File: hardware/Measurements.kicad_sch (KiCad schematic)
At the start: 13 parts, among them IC1 MCP1501-10E_SN, IC3 REF193GSZ-REEL, IC7 MCP3562T-E_NC

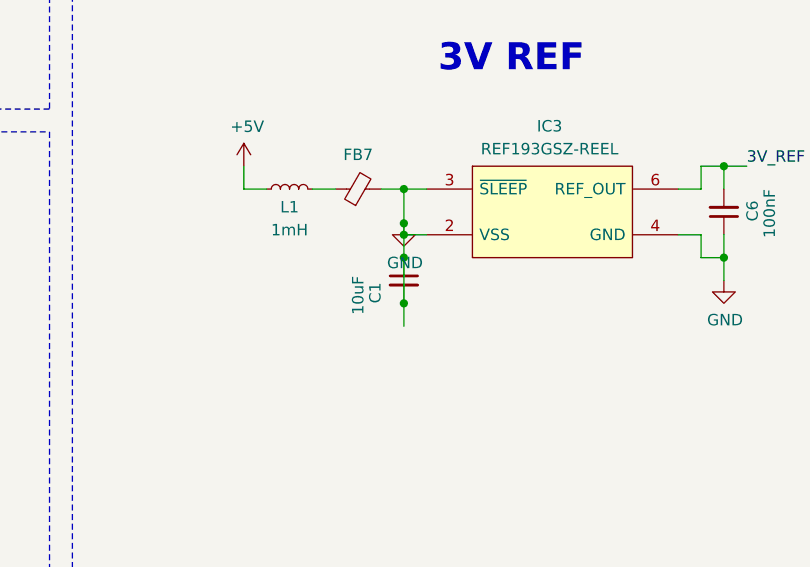
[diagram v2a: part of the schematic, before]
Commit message: relay new driving logic, some ltc communication changes
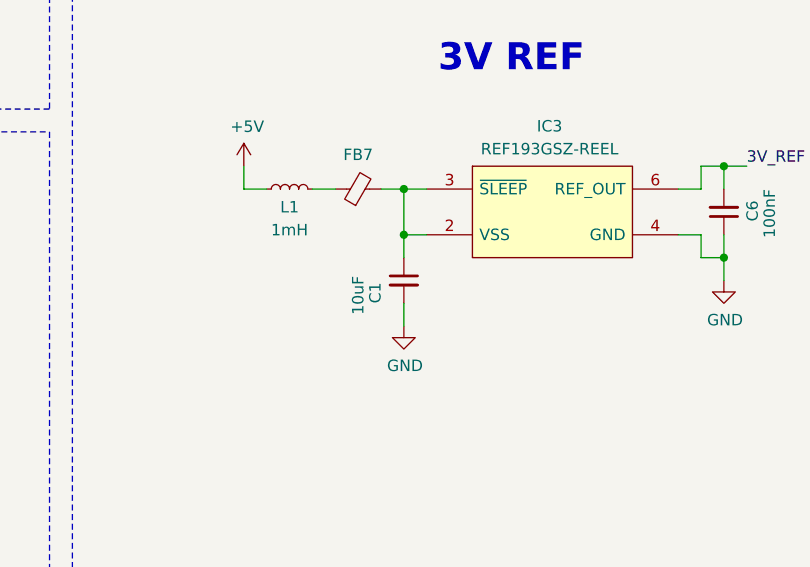
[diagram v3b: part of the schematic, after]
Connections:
- net GND: no longer C1.1, FB7.2, IC3.2 (VSS), IC3.3 (~{SLEEP})
- new net: C1.1, FB7.2, IC3.2 (VSS), IC3.3 (~{SLEEP})
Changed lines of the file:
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@@
-	)
-	(junction
-		(at 213.36 124.46)
-		(diameter 0)
-		(color 0 0 0 0)
-	)
-	(junction
-		(at 213.36 128.27)
-		(diameter 0)
-		(color 0 0 0 0)
 	)
 	(junction
@@
 	)
 	(junction
-		(at 213.36 133.35)
-		(diameter 0)
-		(color 0 0 0 0)
-	)
-	(junction
 		(at 213.36 125.73)
 		(diameter 0)
@@
 	(wire
 		(pts
-			(xy 213.36 133.35) (xy 213.36 128.27)
-		)
-		(stroke
-			(width 0)
-			(type default)
-		)
-	)
-	(wire
-		(pts
 			(xy 246.38 118.11) (xy 248.92 118.11)
 		)
@@
 	(wire
 		(pts
-			(xy 213.36 125.73) (xy 213.36 124.46)
+			(xy 213.36 120.65) (xy 213.36 125.73)
 		)
 		(stroke
@@
 		(pts
 			(xy 76.2 176.53) (xy 78.74 176.53)
-		)
-		(stroke
-			(width 0)
-			(type default)
-		)
-	)
-	(wire
-		(pts
-			(xy 213.36 124.46) (xy 213.36 120.65)
 		)
 		(stroke
@@
 	(symbol
 		(lib_id "power:GND")
-		(at 213.36 124.46 0)
+		(at 213.36 135.89 0)
 		(unit 1)
 		(exclude_from_sim no)
@@
 		(dnp no)
 		(property "Reference" "#PWR023"
-			(at 213.36 130.81 0)
+			(at 213.36 142.24 0)
 			(effects
 				(font
@@
 		)
 		(property "Value" "GND"
-			(at 213.487 128.8542 0)
+			(at 213.487 140.2842 0)
 			(effects
 				(font
@@
 		)
 		(property "Footprint" ""
-			(at 213.36 124.46 0)
+			(at 213.36 135.89 0)
 			(effects
 				(font
@@
 		)
 		(property "Datasheet" ""
-			(at 213.36 124.46 0)
+			(at 213.36 135.89 0)
 			(effects
 				(font
@@
 		)
 		(property "Description" ""
-			(at 213.36 124.46 0)
-			(effects
-				(font
+			(at 213.36 135.89 0)
+			(effects
+				(font

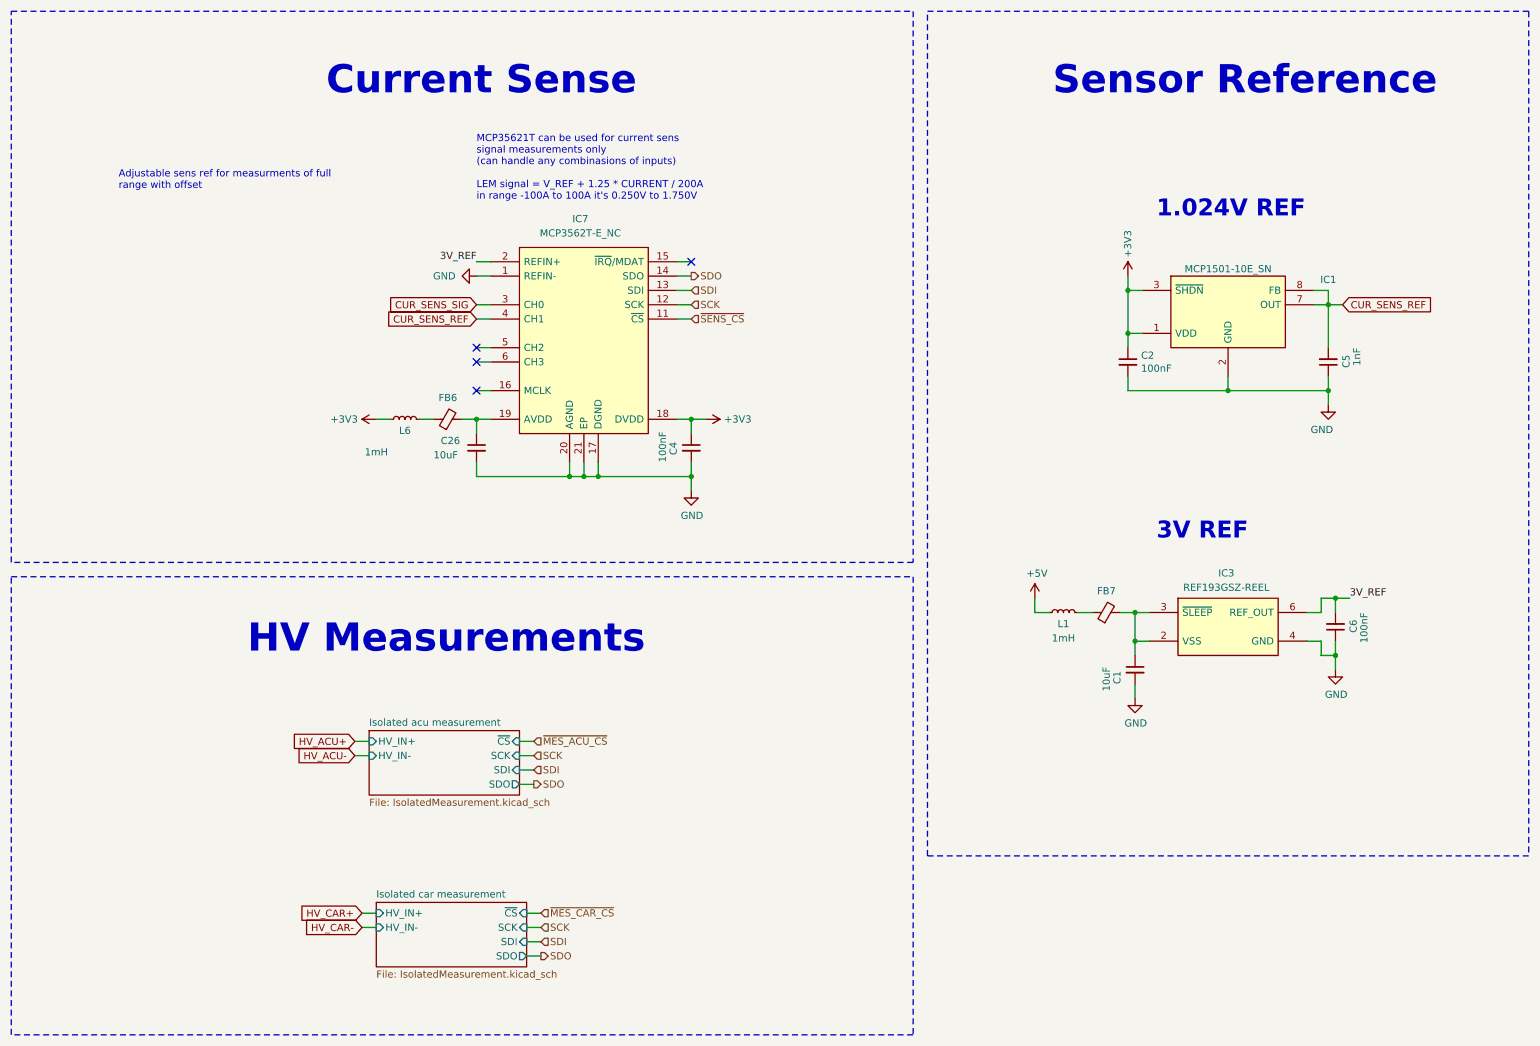
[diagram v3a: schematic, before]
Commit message: relay new driving logic, some ltc communication changes
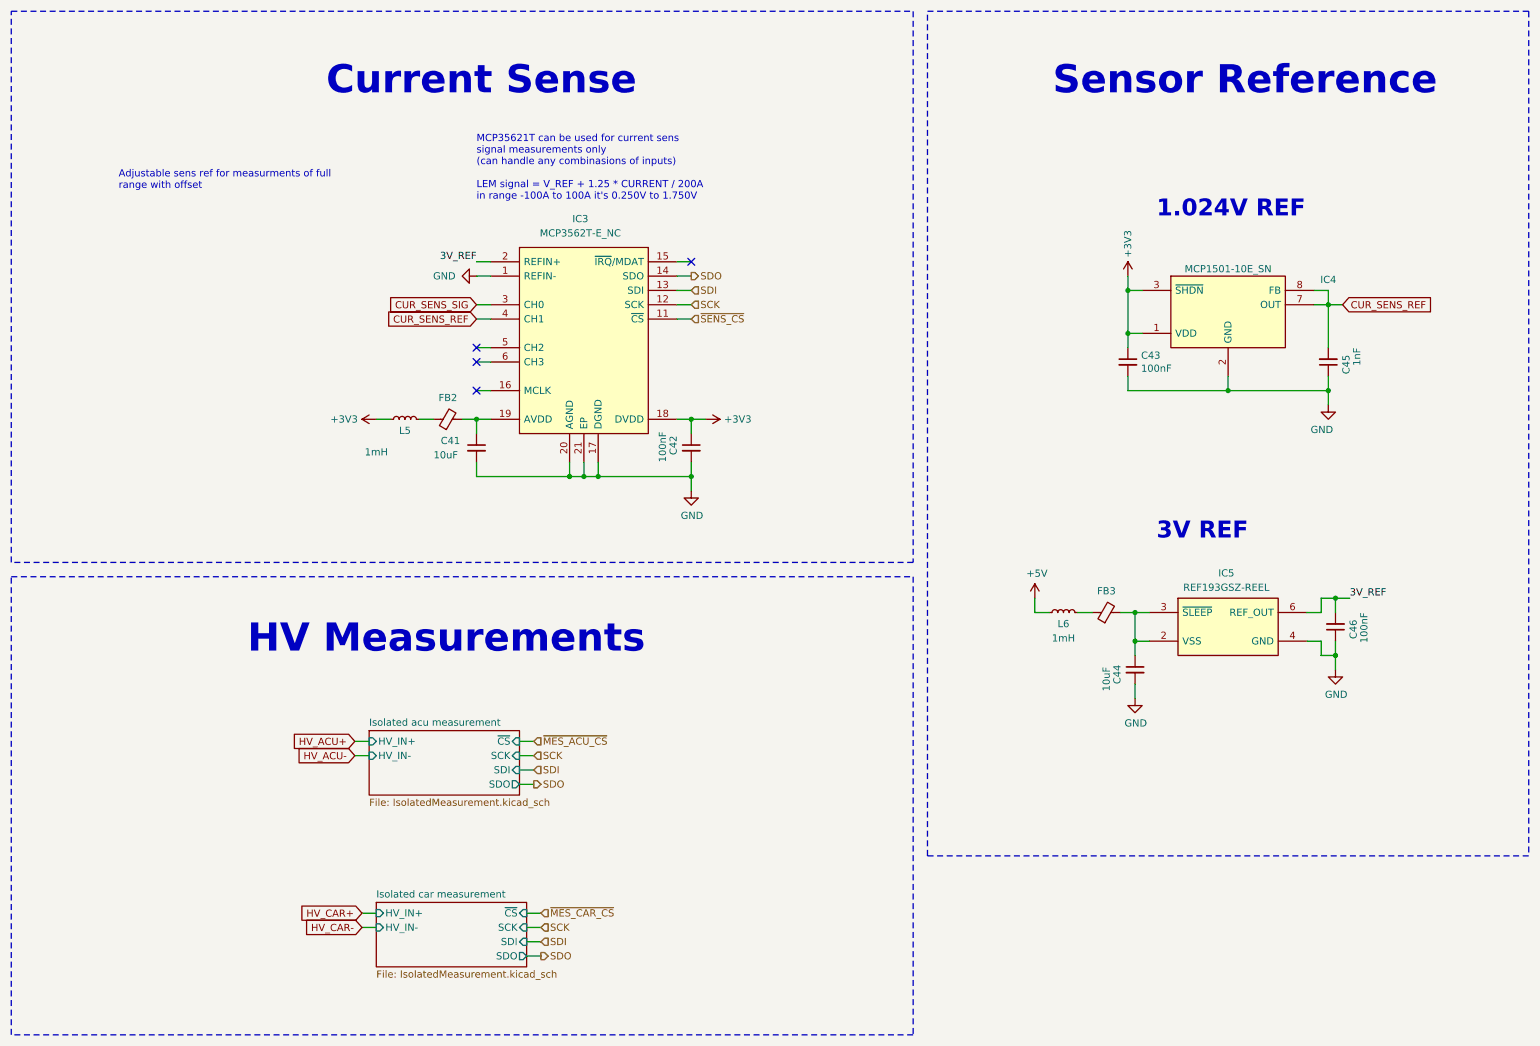
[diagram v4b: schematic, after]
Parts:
- renumbered C26 to C41, C4 to C42, C2 to C43, C1 to C44, C5 to C45, C6 to C46, FB6 to FB2, FB7 to FB3, IC7 to IC3, IC1 to IC4, IC3 to IC5, L6 to L5, L1 to L6
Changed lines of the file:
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@@
 		(on_board yes)
 		(dnp no)
-		(property "Reference" "C1"
+		(property "Reference" "C44"
 			(at 210.185 133.35 90)
 			(effects
@@
 			(project "PUTM_EV_BMS_HV_Master_2021"
 				(path "/b456cffc-d9d7-4c91-91f2-36ec9a65dd1b/e61cc821-5479-4c04-b5ab-4a32f17b4f03"
-					(reference "C1")
+					(reference "C44")
 					(unit 1)
 				)
@@
 		(on_board yes)
 		(dnp no)
-		(property "Reference" "IC1"
+		(property "Reference" "IC4"
 			(at 247.65 61.595 0)
 			(effects
@@
 			(project "PUTM_EV_BMS_HV_Master_2021"
 				(path "/b456cffc-d9d7-4c91-91f2-36ec9a65dd1b/e61cc821-5479-4c04-b5ab-4a32f17b4f03"
-					(reference "IC1")
+					(reference "IC4")
 					(unit 1)
 				)
@@
 		(on_board yes)
 		(dnp no)
-		(property "Reference" "L6"
+		(property "Reference" "L5"
 			(at 83.82 87.63 90)
 			(effects
@@
 			(project "PUTM_EV_BMS_HV_Master_2021"
 				(path "/b456cffc-d9d7-4c91-91f2-36ec9a65dd1b/e61cc821-5479-4c04-b5ab-4a32f17b4f03"
-					(reference "L6")
+					(reference "L5")
 					(unit 1)
 				)
@@
 		(on_board yes)
 		(dnp no)
-		(property "Reference" "#PWR0184"
+		(property "Reference" "#PWR0121"
 			(at 90.17 60.96 0)
 			(effects
@@
 			(project "PUTM_EV_BMS_HV_Master_2021"
 				(path "/b456cffc-d9d7-4c91-91f2-36ec9a65dd1b/e61cc821-5479-4c04-b5ab-4a32f17b4f03"
-					(reference "#PWR0184")
+					(reference "#PWR0121")
 					(unit 1)
 				)
@@
 		(dnp no)
 		(fields_autoplaced yes)
-		(property "Reference" "IC7"
+		(property "Reference" "IC3"
 			(at 114.935 50.8 0)
 			(effects
@@
 			(project "PUTM_EV_BMS_HV_Master_2021"
 				(path "/b456cffc-d9d7-4c91-91f2-36ec9a65dd1b/e61cc821-5479-4c04-b5ab-4a32f17b4f03"
-					(reference "IC7")
+					(reference "IC3")
 					(unit 1)
 				)
@@
 		(on_board yes)
 		(dnp no)
-		(property "Reference" "#PWR0103"
+		(property "Reference" "#PWR0128"
 			(at 248.92 137.16 0)
 			(effects
@@
 			(project "PUTM_EV_BMS_HV_Master_2021"
 				(path "/b456cffc-d9d7-4c91-91f2-36ec9a65dd1b/e61cc821-5479-4c04-b5ab-4a32f17b4f03"
-					(reference "#PWR0103")
+					(reference "#PWR0128")
 					(unit 1)
 				)
@@
 		(on_board yes)
 		(dnp no)
-		(property "Reference" "FB7"
+		(property "Reference" "FB3"
 			(at 208.28 116.84 90)
 			(effects
@@
 			(project "PUTM_EV_BMS_HV_Master_2021"
 				(path "/b456cffc-d9d7-4c91-91f2-36ec9a65dd1b/e61cc821-5479-4c04-b5ab-4a32f17b4f03"
-					(reference "FB7")
+					(reference "FB3")
 					(unit 1)
 				)
@@
 		(on_board yes)
 		(dnp no)
-		(property "Reference" "#PWR0170"
+		(property "Reference" "#PWR0123"
 			(at 133.35 86.36 0)
 			(effects
@@
 			(project "PUTM_EV_BMS_HV_Master_2021"
 				(path "/b456cffc-d9d7-4c91-91f2-36ec9a65dd1b/e61cc821-5479-4c04-b5ab-4a32f17b4f03"
-					(reference "#PWR0170")
+					(reference "#PWR0123")
 					(unit 1)
 				)
@@
 		(on_board yes)
 		(dnp no)
-		(property "Reference" "FB6"
+		(property "Reference" "FB2"
 			(at 91.44 82.55 90)
 			(effects
@@
 			(project "PUTM_EV_BMS_HV_Master_2021"
 				(path "/b456cffc-d9d7-4c91-91f2-36ec9a65dd1b/e61cc821-5479-4c04-b5ab-4a32f17b4f03"
-					(reference "FB6")
+					(reference "FB2")
 					(unit 1)
 				)
@@
 		(on_board yes)
 		(dnp no)
-		(property "Reference" "C4"
+		(property "Reference" "C42"
 			(at 131.445 92.71 90)
 			(effects
@@
 			(project "PUTM_EV_BMS_HV_Master_2021"
 				(path "/b456cffc-d9d7-4c91-91f2-36ec9a65dd1b/e61cc821-5479-4c04-b5ab-4a32f17b4f03"
-					(reference "C4")
+					(reference "C42")
 					(unit 1)
 				)
@@
 		(on_board yes)
 		(dnp no)
-		(property "Reference" "#PWR0174"
+		(property "Reference" "#PWR0122"
 			(at 134.62 105.41 0)
 			(effects
@@
 			(project "PUTM_EV_BMS_HV_Master_2021"
 				(path "/b456cffc-d9d7-4c91-91f2-36ec9a65dd1b/e61cc821-5479-4c04-b5ab-4a32f17b4f03"
-					(reference "#PWR0174")
+					(reference "#PWR0122")
 					(unit 1)
 				)
@@
 		(on_board yes)
 		(dnp no)
-		(property "Reference" "C6"
+		(property "Reference" "C46"
 			(at 252.095 121.92 90)
 			(effects
@@
 			(project "PUTM_EV_BMS_HV_Master_2021"
 				(path "/b456cffc-d9d7-4c91-91f2-36ec9a65dd1b/e61cc821-5479-4c04-b5ab-4a32f17b4f03"
-					(reference "C6")
+					(reference "C46")
 					(unit 1)
 				)
@@
 		(on_board yes)
 		(dnp no)
-		(property "Reference" "#PWR0169"
+		(property "Reference" "#PWR0127"
 			(at 247.65 90.17 0)
 			(effects
@@
 			(project "PUTM_EV_BMS_HV_Master_2021"
 				(path "/b456cffc-d9d7-4c91-91f2-36ec9a65dd1b/e61cc821-5479-4c04-b5ab-4a32f17b4f03"
-					(reference "#PWR0169")
+					(reference "#PWR0127")
 					(unit 1)
 				)
@@
 		(on_board yes)
 		(dnp no)
-		(property "Reference" "#PWR0167"
+		(property "Reference" "#PWR0125"
 			(at 212.09 64.77 0)
 			(effects
@@
 			(project "PUTM_EV_BMS_HV_Master_2021"
 				(path "/b456cffc-d9d7-4c91-91f2-36ec9a65dd1b/e61cc821-5479-4c04-b5ab-4a32f17b4f03"
-					(reference "#PWR0167")
+					(reference "#PWR0125")
 					(unit 1)
 				)
@@
 		(on_board yes)
 		(dnp no)
-		(property "Reference" "C5"
+		(property "Reference" "C45"
 			(at 250.825 74.93 90)
 			(effects
@@
 			(project "PUTM_EV_BMS_HV_Master_2021"
 				(path "/b456cffc-d9d7-4c91-91f2-36ec9a65dd1b/e61cc821-5479-4c04-b5ab-4a32f17b4f03"
-					(reference "C5")
+					(reference "C45")
 					(unit 1)
 				)
@@
 		(on_board yes)
 		(dnp no)
-		(property "Reference" "L1"
+		(property "Reference" "L6"
 			(at 200.66 121.92 90)
 			(effects
@@
 			(project "PUTM_EV_BMS_HV_Master_2021"
 				(path "/b456cffc-d9d7-4c91-91f2-36ec9a65dd1b/e61cc821-5479-4c04-b5ab-4a32f17b4f03"
-					(reference "L1")
+					(reference "L6")
 					(unit 1)
 				)
@@
 		(on_board yes)
 		(dnp no)
-		(property "Reference" "C2"
+		(property "Reference" "C43"
 			(at 214.4268 75.0316 0)
 			(effects
@@
 			(project "PUTM_EV_BMS_HV_Master_2021"
 				(path "/b456cffc-d9d7-4c91-91f2-36ec9a65dd1b/e61cc821-5479-4c04-b5ab-4a32f17b4f03"
-					(reference "C2")
+					(reference "C43")
 					(unit 1)
 				)
@@
 		(on_board yes)
 		(dnp no)
-		(property "Reference" "C26"
+		(property "Reference" "C41"
 			(at 90.17 90.17 0)
 			(effects
@@
 			(project "PUTM_EV_BMS_HV_Master_2021"
 				(path "/b456cffc-d9d7-4c91-91f2-36ec9a65dd1b/e61cc821-5479-4c04-b5ab-4a32f17b4f03"
-					(reference "C26")
+					(reference "C41")
 					(unit 1)
 				)
@@
 		(on_board yes)
 		(dnp no)
-		(property "Reference" "#PWR0104"
+		(property "Reference" "#PWR0124"
 			(at 195.58 121.92 0)
 			(effects
@@
 			(project "PUTM_EV_BMS_HV_Master_2021"
 				(path "/b456cffc-d9d7-4c91-91f2-36ec9a65dd1b/e61cc821-5479-4c04-b5ab-4a32f17b4f03"
-					(reference "#PWR0104")
+					(reference "#PWR0124")
 					(unit 1)
 				)
@@
 		(on_board yes)
 		(dnp no)
-		(property "Reference" "#PWR0158"
+		(property "Reference" "#PWR0120"
 			(at 82.55 86.36 0)
 			(effects
@@
 			(project "PUTM_EV_BMS_HV_Master_2021"
 				(path "/b456cffc-d9d7-4c91-91f2-36ec9a65dd1b/e61cc821-5479-4c04-b5ab-4a32f17b4f03"
-					(reference "#PWR0158")
+					(reference "#PWR0120")
 					(unit 1)
 				)
@@
 		(dnp no)
 		(fields_autoplaced yes)
-		(property "Reference" "IC3"
+		(property "Reference" "IC5"
 			(at 229.5525 113.665 0)
 			(effects
@@
 			(project "PUTM_EV_BMS_HV_Master_2021"
 				(path "/b456cffc-d9d7-4c91-91f2-36ec9a65dd1b/e61cc821-5479-4c04-b5ab-4a32f17b4f03"
-					(reference "IC3")
+					(reference "IC5")
 					(unit 1)
 				)
@@
 		(on_board yes)
 		(dnp no)
-		(property "Reference" "#PWR023"
+		(property "Reference" "#PWR0126"
 			(at 213.36 142.24 0)
 			(effects
@@
 			(project "PUTM_EV_BMS_HV_Master_2021"
 				(path "/b456cffc-d9d7-4c91-91f2-36ec9a65dd1b/e61cc821-5479-4c04-b5ab-4a32f17b4f03"
-					(reference "#PWR023")
-					(unit 1)
-				)
+					(reference "#PWR0126")
+					(unit 1)
+				)

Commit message: major schematic changes
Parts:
- removed C41, C44: 10uF, Capacitor_SMD:C_0603_1608Metric, symbol Device:C_Small
- removed C42, C43, C46: 100nF, Capacitor_SMD:C_0603_1608Metric, symbol Device:C_Small
- removed C45: 1nF, Capacitor_SMD:C_0603_1608Metric, symbol Device:C_Small
- removed FB2, FB3: GZ1608D601TF, Inductor_SMD:L_0603_1608Metric, symbol Device:Ferrite_Bead_Small
- removed IC3: MCP3562T-E_NC, MCP3561T-E_NC:QFN40P300X300X60-21N-D, symbol MCP3562T-E_NC:MCP3562T-E_NC
- removed IC4: MCP1501-10E_SN, MCP1501-10E_SN:SOIC127P600X175-8N, symbol MCP1501-10E_SN:MCP1501-10E_SN
- removed IC5: REF193GSZ-REEL, MCP1501-10E_SN:SOIC127P600X175-8N, symbol REF196GSZ-REEL:REF196GSZ-REEL
- removed L5, L6: 1mH, Inductor_SMD:L_1206_3216Metric, symbol Device:L_Small
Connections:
- no-connect marks 4 -> 0
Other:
- removed sheet Isolated acu measurement
- removed sheet Isolated car measurement
- note removed: "1.024V REF"
- note removed: "3V REF"
- note removed: "Adjustable sens ref for measurments of full range with offset"
- note removed: "Current Sense"
- note removed: "HV Measurements"
- note removed: "MCP35621T can be used for current sens signal measurements only (can handle any combinasions of inputs) LEM signal = V_REF + 1.25 * CURRENT / 200A in range -100A to 100A it's 0.250V to 1.750V"
- note removed: "Sensor Reference"
